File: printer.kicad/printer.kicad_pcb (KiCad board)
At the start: 2 copper layers, 74 x 47 mm, 34 parts, among them J1 ZX_Spectrum_128K_expansion, J2 Conn_01x06_Male, J3 Conn_01x05_Male, J4 Conn_01x04_Male, U1 SN74AHC373, U2 SN74HCT00, U3 SN74AHCT02, U4 SN74AHC373, U5 XC6206PxxxMR, U6 STM32F103C8Tx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

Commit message: Add banner and JLCPCB number placeholder
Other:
- board text added: "JLCJLCJLCJLC"
- board text added: "Thermal Spectrum v1 by spbnick"
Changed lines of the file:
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@@
   (general
     (thickness 1.6)
-    (drawings 35)
+    (drawings 55)
     (tracks 608)
     (zones 0)
@@
     )
   )
+  (gr_text JLCJLCJLCJLC (at 146.05 120.1) (layer B.SilkS)
+    (effects (font (size 1 1) (thickness 0.15)) (justify mirror))
+  )
+  (gr_text "Thermal Spectrum\nv1 by spbnick" (at 126.7 102.3) (layer F.SilkS)
+    (effects (font (size 1 1) (thickness 0.15)))
+  )
+  (gr_line (start 128 97.25) (end 128.9 97.25) (layer F.SilkS) (width 0.12))
+  (gr_line (start 127.8 97.75) (end 128.7 97.75) (layer F.SilkS) (width 0.12))
+  (gr_line (start 127.6 98.25) (end 128.5 98.25) (layer F.SilkS) (width 0.12))
+  (gr_line (start 127.5 98.75) (end 128.4 98.75) (layer F.SilkS) (width 0.12))
+  (gr_line (start 127.1 99.75) (end 128 99.75) (layer F.SilkS) (width 0.12))
+  (gr_line (start 127.3 99.25) (end 128.2 99.25) (layer F.SilkS) (width 0.12))
+  (gr_line (start 126.2 99.5) (end 128.1 99.5) (layer F.SilkS) (width 0.12))
+  (gr_line (start 126.6 98.5) (end 128.5 98.5) (layer F.SilkS) (width 0.12))
+  (gr_line (start 126.9 97.5) (end 128.8 97.5) (layer F.SilkS) (width 0.12))
+  (gr_line (start 128.3 99) (end 125.4 99) (layer F.SilkS) (width 0.12))
+  (gr_line (start 125.7 98) (end 128.6 98) (layer F.SilkS) (width 0.12))
+  (gr_line (start 128 97) (end 127 100) (layer F.SilkS) (width 0.12))
+  (gr_line (start 127 97) (end 126 100) (layer F.SilkS) (width 0.12))
+  (gr_line (start 126 97) (end 125 100) (layer F.SilkS) (width 0.12))
+  (gr_line (start 128 100) (end 124 100) (layer F.SilkS) (width 0.12))
+  (gr_line (start 129 97) (end 128 100) (layer F.SilkS) (width 0.12))
+  (gr_line (start 125 97) (end 129 97) (layer F.SilkS) (width 0.12))
+  (gr_line (start 124 100) (end 125 97) (layer F.SilkS) (width 0.12))
   (gr_circle (center 144.8 89.3) (end 145 89.3) (layer F.SilkS) (width 0.4))
   (gr_line (start 113.1 89.8) (end 112.8 89.5) (layer F.SilkS) (width 0.12))

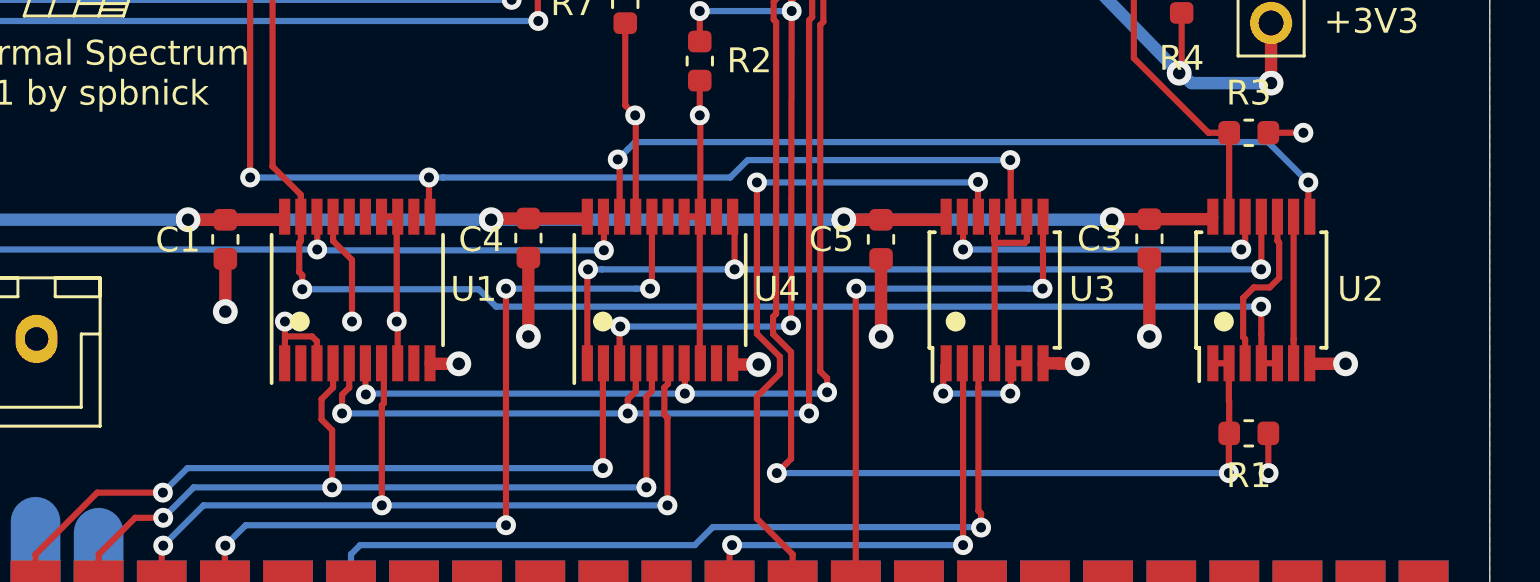
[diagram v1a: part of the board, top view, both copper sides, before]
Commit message: Switch to parts in stock at LCSC
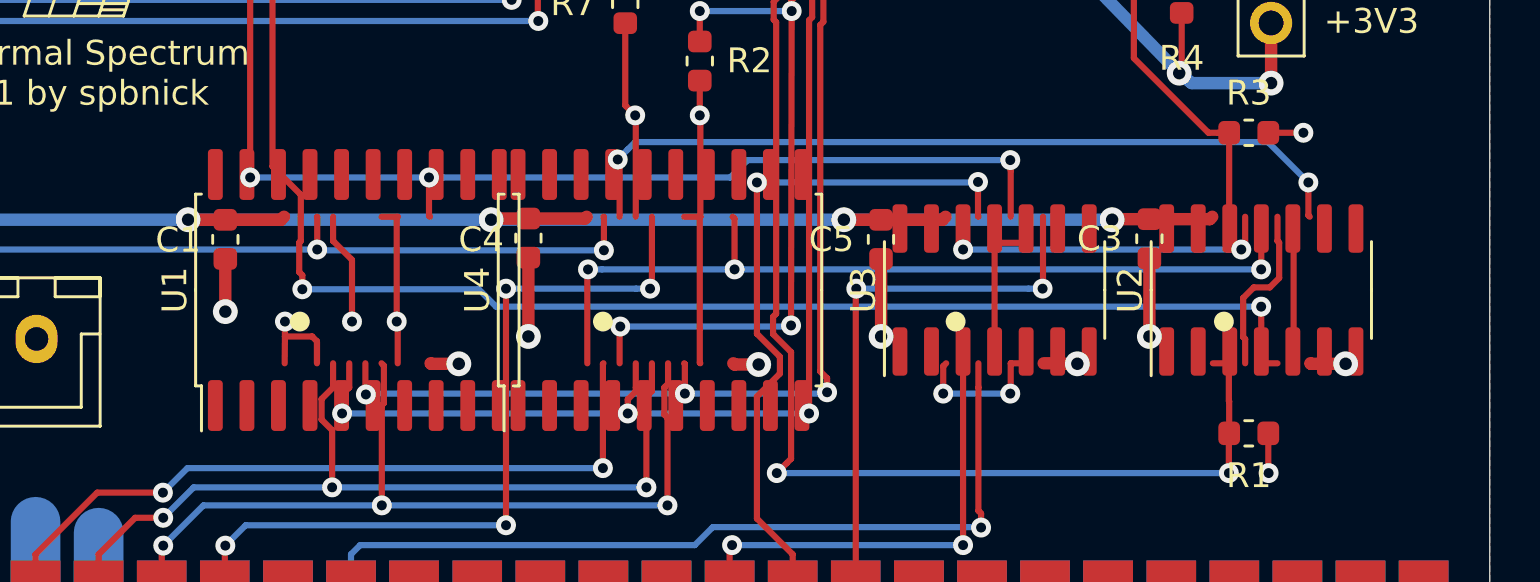
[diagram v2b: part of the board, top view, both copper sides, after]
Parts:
- U1, U4: value SN74AHC373 -> SN74HCT373DWR; footprint Package_SO:TSSOP-20_4.4x6.5mm_P0.65mm -> Package_SO:SOIC-20W_7.5x12.8mm_P1.27mm
- U2: value SN74HCT00 -> SN74HCT00DR; footprint Package_SO:TSSOP-14_4.4x5mm_P0.65mm -> Package_SO:SOIC-14_3.9x8.7mm_P1.27mm
- U3: value SN74AHCT02 -> SN74HCT02DRG4; footprint Package_SO:TSSOP-14_4.4x5mm_P0.65mm -> Package_SO:SOIC-14_3.9x8.7mm_P1.27mm
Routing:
- net Net-(U2-Pad8): track 32.5 -> 0.00 mm, vias 2 -> 0
- net GND: track 107.0 -> 138.2 mm, vias 24 -> 25
- net /~RD: track 29.5 -> 43.4 mm, vias 2 -> 4
- net /READ: track 13.9 -> 0.00 mm, vias 2 -> 0
- net Net-(U3-Pad1): track 5.85 -> 7.21 mm, vias 2 -> 3

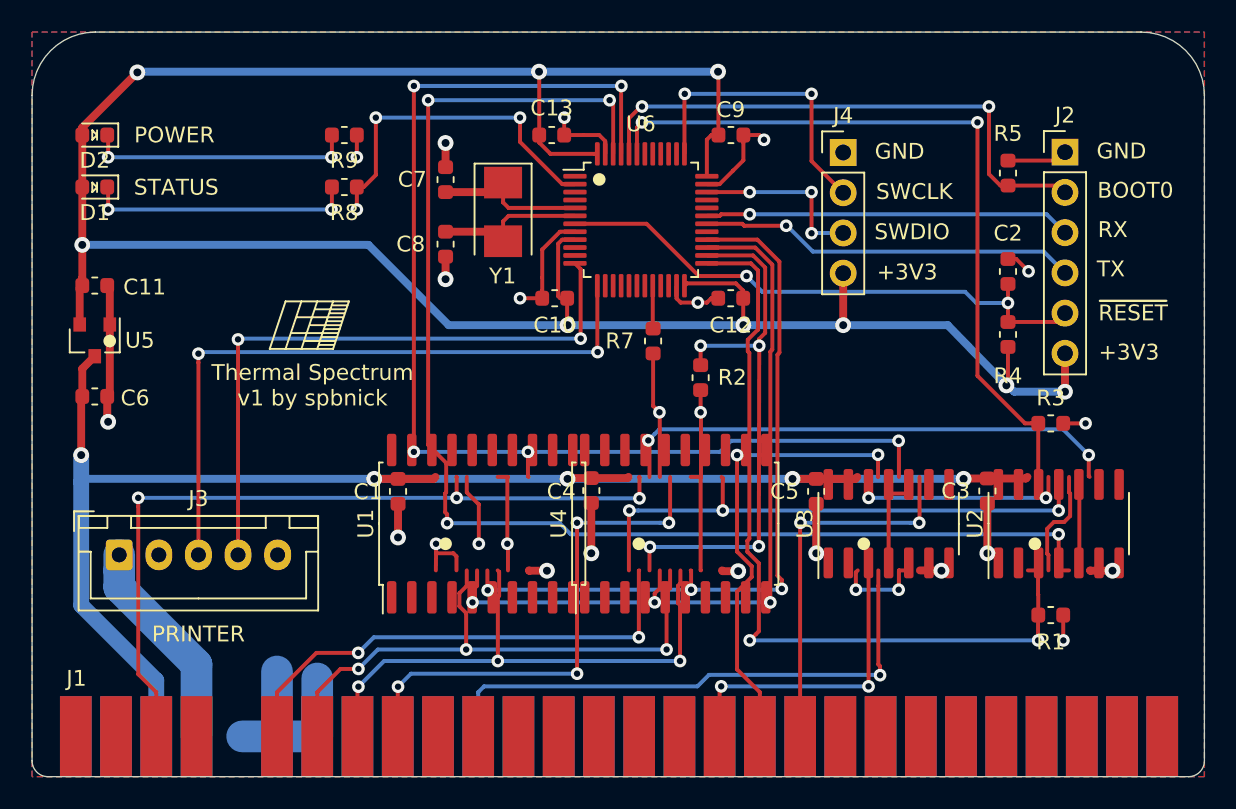
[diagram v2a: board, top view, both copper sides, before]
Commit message: Reroute with new footprints and top ground fill
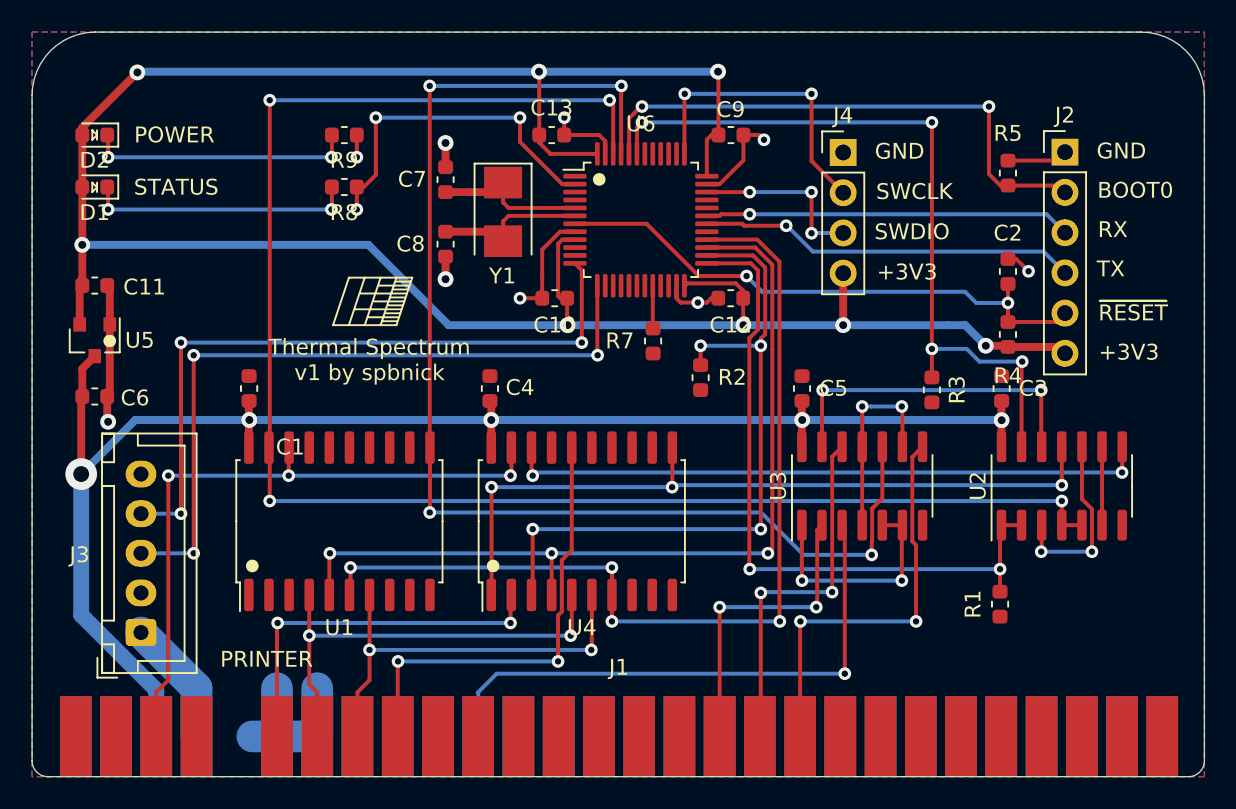
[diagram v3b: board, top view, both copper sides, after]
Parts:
- moved C1 11.4 mm to (122.7, 102.5), turned to 90 degrees
- moved C4 9.08 mm to (137.9, 102.5), turned to 90 degrees
- moved U1 9.02 mm to (128.4, 110.9)
- moved R3 7.79 mm to (165.8, 102.6), turned to 270 degrees
- moved C5 6.55 mm to (157.6, 102.5), turned to 90 degrees
- moved C3 6.53 mm to (170.2, 102.5), turned to 90 degrees
- moved U4 5.90 mm to (143.7, 110.9)
- moved J3 5.09 mm to (115.9, 117.9), turned to 90 degrees
- moved R1 3.27 mm to (170.1, 116.1), turned to 270 degrees
- moved U3 2.91 mm to (161.4, 108.7)
- moved U2 2.39 mm to (174.0, 108.7)
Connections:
- net Net-(U2-Pad11) renamed /OUTPUT
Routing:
- net GND: track 138.2 -> 50.0 mm, vias 25 -> 9
- net Net-(U2-Pad8): track 0.00 -> 40.7 mm, vias 0 -> 2
- net /READ: track 0.00 -> 21.0 mm, vias 0 -> 2
- net /~RD: track 43.4 -> 23.0 mm, vias 4 -> 2
- net /STYLUS: track 84.0 -> 103.1 mm
- net /MOTOR_OFF: track 47.1 -> 60.4 mm, vias 3 -> 4
- net /OUTPUT: track 35.2 -> 47.8 mm
- net /ENCODER: track 35.1 -> 44.2 mm
- net /D2: track 35.8 -> 26.7 mm, vias 3 -> 2
- net /D1: track 36.4 -> 28.2 mm, vias 3 -> 2
- net /D7: track 49.9 -> 41.9 mm
- net /D0: track 31.3 -> 23.7 mm
- net Net-(U3-Pad1): track 7.21 -> 14.6 mm, vias 3 -> 2
- net /PAPER: track 51.0 -> 43.8 mm
- net /MOTOR_SLOW: track 49.2 -> 55.8 mm
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- added copper zone on F.Cu, net GND
- removed copper zone on F.Cu, net (none)

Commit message: Improve ground connectivity and reduce loops
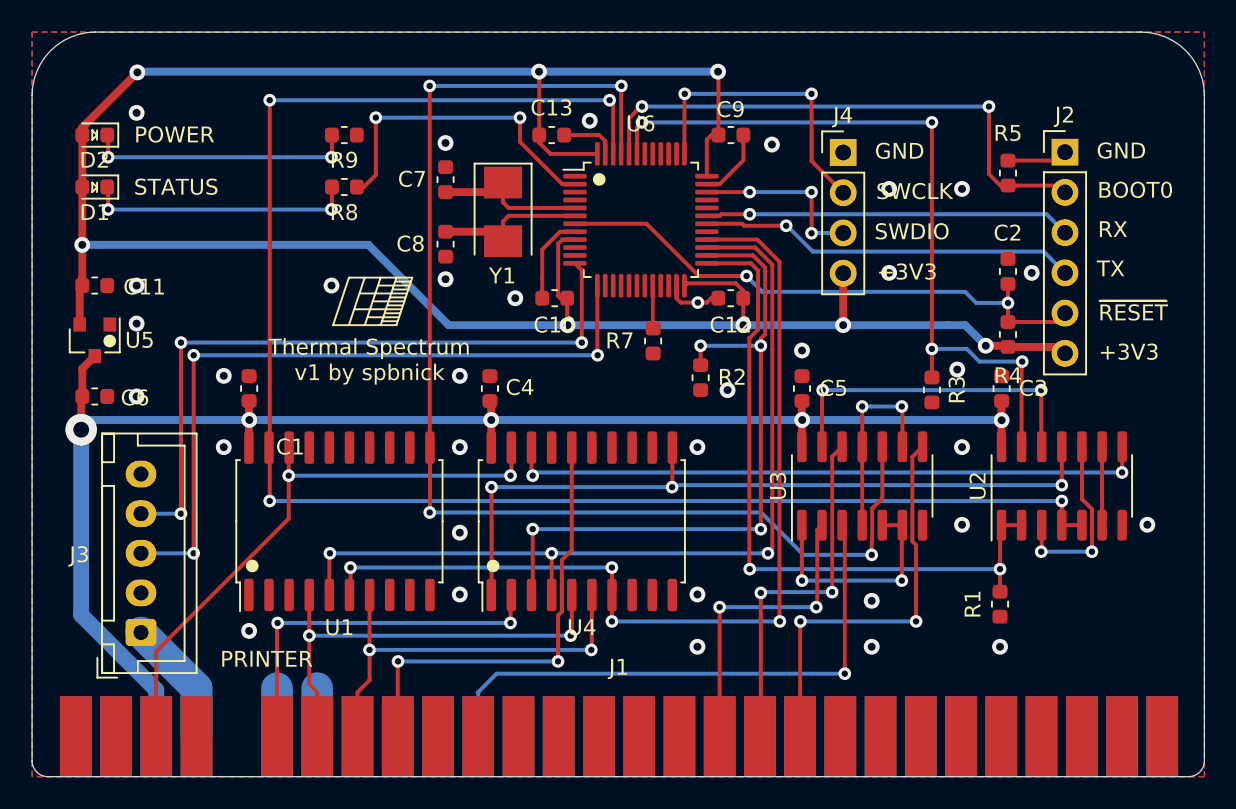
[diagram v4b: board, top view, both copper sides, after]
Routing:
- net GND: track 50.0 -> 28.6 mm, vias 9 -> 34
- net /D7: track 41.9 -> 37.5 mm, vias 3 -> 2
- net /STATUS_LED: track 21.8 -> 20.3 mm, vias 3 -> 2
- net +5V: track 97.6 -> 96.4 mm
